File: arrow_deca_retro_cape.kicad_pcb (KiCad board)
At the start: 2 copper layers, 100 x 100 mm, 84 parts, among them J1 DB15_Female_HighDensity_Mount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, J10 Conn_02x06_Odd_Even, J11 PMOD1, J12 PMOD2, J14 Conn_01x02, J15 Conn_01x03, J16 Conn_01x06, J17 Conn_01x02, J18 Conn_01x03, J19 DINC_MIN_TM_6_1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

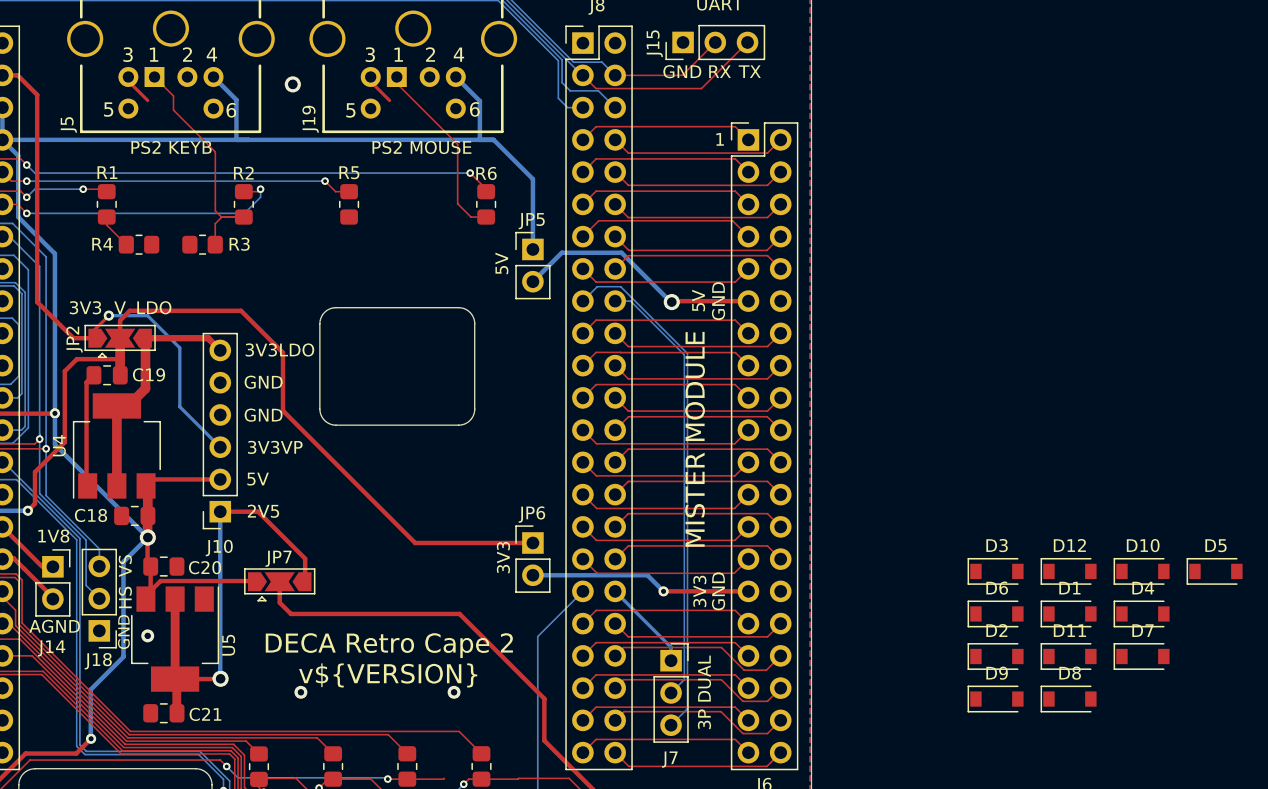
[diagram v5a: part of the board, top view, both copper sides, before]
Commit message: v0.78 ps2 protections with zeners
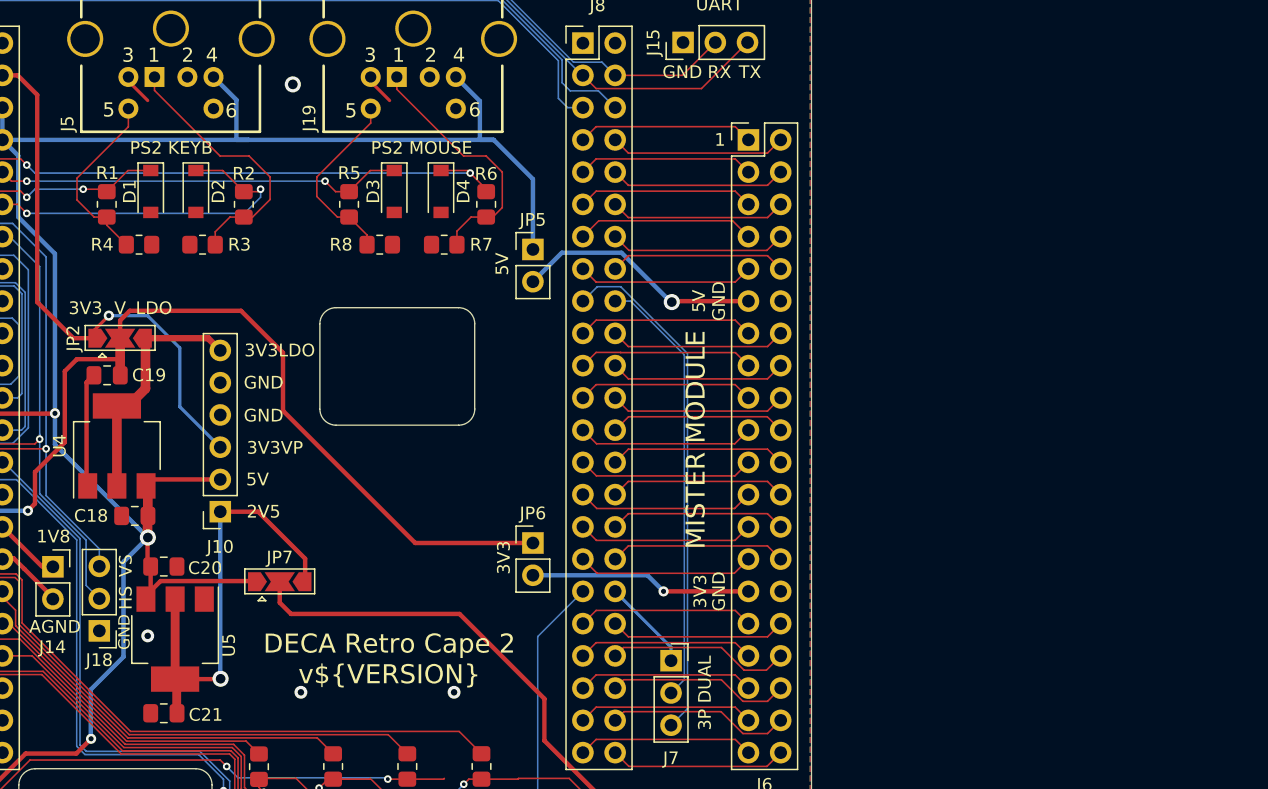
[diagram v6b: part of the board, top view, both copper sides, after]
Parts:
- removed D10, D11, D5, D6, D7, D8, D9: MMSZ5221BT1G, Diode_SMD:D_SOD-123
- removed D12: MMSZ5225BG, Diode_SMD:D_SOD-123
- added R7: DNI 4k7, Resistor_SMD:R_0805_2012Metric_Pad1.20x1.40mm_HandSolder, F.Cu at (154.2, 61.6)
- added R8: DNI 4k7, Resistor_SMD:R_0805_2012Metric_Pad1.20x1.40mm_HandSolder, F.Cu at (149.1, 61.6)
- D1, D2, D3, D4: value MMSZ5225BG -> BZT52C3V9
- moved D1 79.7 mm to (131.1, 57.4), turned to -90 degrees
- moved D2 72.9 mm to (134.6, 57.4), turned to -90 degrees
- moved D4 64.5 mm to (153.9, 57.4), turned to -90 degrees
- moved D3 56.1 mm to (150.2, 57.4), turned to -90 degrees
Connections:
- J12 pad 10: unconnected-(J12-Pad10) -> /DETO2
- J12 pad 7: unconnected-(J12-Pad7) -> /VGA_HS
- J12 pad 8: unconnected-(J12-Pad8) -> /VGA_VS
- J12 pad 9: unconnected-(J12-Pad9) -> /DETO1
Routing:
- net Net-(J19-Pad5): track 0.00 -> 14.7 mm
- net Net-(J5-Pad5): track 2.81 -> 14.6 mm
- net Net-(J19-Pad1): track 14.6 -> 20.2 mm
- net /PS2_KEYB_DAT: track 23.2 -> 27.7 mm
- net /PS2_MOUSE_CLK: track 27.9 -> 32.2 mm
- net /PS2_KEYB_CLK: track 11.7 -> 15.8 mm
- net /PS2_MOUSE_DAT: track 42.3 -> 44.6 mm
- net Net-(J5-Pad1): track 19.1 -> 21.1 mm

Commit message: v0.80 WIP adding level shifter for db9/usb3
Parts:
- added JP8: Conn_01x03, Connector_PinHeader_2.54mm:PinHeader_1x03_P2.54mm_Vertical, F.Cu at (148.0, 88.1)
- added U1: TXS0108EPW, Package_SO:TSSOP-20_4.4x6.5mm_P0.65mm, F.Cu at (148.1, 94.9)
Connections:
- J21 pad 1: +5V -> /+JOY_PWR_USB3
- J4 pad 5: /+JOY_PWR -> /+JOY_PWR_DB9
- R10 pad 1: /JOY1_RIGHT -> Net-(R10-Pad1)
- R11 pad 1: /JOY1_LEFT -> Net-(R11-Pad1)
- R12 pad 1: /JOYX_SEL_O -> Net-(R12-Pad1)
- R13 pad 1: /JOY1_DOWN -> Net-(R13-Pad1)
- R14 pad 1: /JOY1_B1_P6 -> Net-(R14-Pad1)
- R15 pad 1: /JOY1_UP -> Net-(R15-Pad1)
- R9 pad 1: /JOY1_B2_P9 -> Net-(R9-Pad1)
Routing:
- net /+JOY_PWR_USB3: track 0.00 -> 63.8 mm, vias 0 -> 1
- net +5V: track 210.1 -> 155.3 mm, vias 4 -> 3
- net Net-(R15-Pad1): track 0.00 -> 48.3 mm
- net /JOY1_UP: track 48.3 -> 0.00 mm
- net Net-(R9-Pad1): track 0.00 -> 42.6 mm
- net /JOY1_B2_P9: track 42.6 -> 0.00 mm
- net /+JOY_PWR_DB9: track 0.00 -> 38.3 mm
- net /+JOY_PWR: track 51.0 -> 12.9 mm
- net Net-(R13-Pad1): track 0.00 -> 24.5 mm
- net /JOY1_DOWN: track 24.5 -> 0.00 mm
- net GND: track 43.7 -> 21.0 mm, vias 7 -> 5
- net /TX-: track 116.5 -> 95.4 mm
- net /DRAIN: track 114.3 -> 102.3 mm
- net /RX+: track 107.9 -> 96.4 mm
- net /D-: track 105.0 -> 94.4 mm
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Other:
- board text added: "**"
- board text added: "SELECT"
- board text added: "USB3"
- board text added: "USB3 USER IO"
- board text removed: "USER PORT"

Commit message: v0.8 routing ended for level shifter
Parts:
- JP3: moved to F.Cu
- moved R16 38.1 mm to (165.4, 136.4), turned to 90 degrees
- moved R13 13.9 mm to (153.4, 104.1), turned to 0 degrees
- moved R10 13.6 mm to (153.4, 97.3), turned to 0 degrees
- moved U1 9.09 mm to (144.3, 103.1)
- moved R11 8.94 mm to (153.4, 99.6), turned to 0 degrees
- moved R14 8.78 mm to (153.4, 106.3), turned to 0 degrees
- moved R9 7.99 mm to (153.4, 95.0), turned to 0 degrees
- moved JP3 4.07 mm to (165.4, 130.7), turned to 90 degrees
- moved R12 3.79 mm to (153.4, 101.9), turned to 0 degrees
- moved R15 3.70 mm to (153.4, 108.5), turned to 0 degrees
- moved LO1 2.26 mm to (141.2, 57.4)
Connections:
- net Net-(J22-Pad1) renamed /TX+b
- U1 pad 1: /JOY1_B2_P9 -> unconnected-(U1-Pad1)
- U1 pad 17: unconnected-(U1-Pad17) -> Net-(R10-Pad1)
- U1 pad 18: Net-(R10-Pad1) -> Net-(R9-Pad1)
- U1 pad 20: Net-(R9-Pad1) -> unconnected-(U1-Pad20)
- U1 pad 3: /JOY1_RIGHT -> /JOY1_B2_P9
- U1 pad 4: unconnected-(U1-Pad4) -> /JOY1_RIGHT
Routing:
- net Net-(R15-Pad1): track 48.3 -> 7.53 mm
- net /JOY1_B2_P9: track 0.00 -> 32.7 mm
- net Net-(R9-Pad1): track 42.6 -> 10.1 mm
- net Net-(JP3-Pad1): track 35.8 -> 4.08 mm, vias 1 -> 0
- net /JOY1_UP: track 0.00 -> 30.4 mm
- net /JOY1_DOWN: track 0.00 -> 27.7 mm, vias 0 -> 2
- net /DETO3_JOY_MUX: track 55.5 -> 82.1 mm, vias 1 -> 3
- net Net-(R13-Pad1): track 24.5 -> 5.30 mm
- net +2V5: track 35.9 -> 52.7 mm
- net /TX-: track 95.4 -> 110.3 mm
- net /D-: track 94.4 -> 108.2 mm
- net /JOY1_LEFT: track 38.9 -> 25.7 mm, vias 0 -> 2
- net /RX+: track 96.4 -> 108.9 mm
- net /LDQM: track 40.7 -> 52.7 mm
- net /+JOY_PWR: track 12.9 -> 24.5 mm
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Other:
- board text added: "MUX(3)"
- board text added: "SCART"
- board text added: "USER IO SELECT"
- board text removed: "JOY_MUX(3)"
